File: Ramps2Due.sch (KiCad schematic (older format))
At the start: 24 parts, among them J1 HEADER_2, J10 HEADER_2, J11 HEADER_8, J12 HEADER_10, J13 HEADER_8, J14 HEADER_8, J15 HEADER_7, J2 HEADER_3X2, J3 HEADER_8, J4 HEADER_8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

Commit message: All the tracts added (I think)
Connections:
- net labels added: V_IN
- net labels removed: +12V, AM-VIN, AM_VIN
- wire segments 169 -> 172

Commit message: Add Open-Source Hardware logo, shrink board edges, remove extraneous tracts.
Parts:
- added M1: LOGO_OSHW, OSHW_logo_2, symbol LOGO_OSHW
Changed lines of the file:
@@
-EESchema Schematic File Version 2  date Thu 28 Feb 2013 03:48:15 PM EST
+EESchema Schematic File Version 2  date Thu 28 Feb 2013 05:09:04 PM EST
 LIBS:power
 LIBS:device
@@
 Comment4 ""
 $EndDescr
+$Comp
+L LOGO_OSHW M1
+U 1 1 512FD565
+P 7250 4600
+F 0 "M1" H 7250 4750 60  0000 C CNN
+F 1 "LOGO_OSHW" H 7250 4500 60  0000 C CNN
+F 2 "OSHW_logo_2" H 7150 4650 60  0000 C CNN
+	1    7250 4600
+	1    0    0    -1
+$EndComp
 Wire Wire Line
 	1000 4800 1150 4800

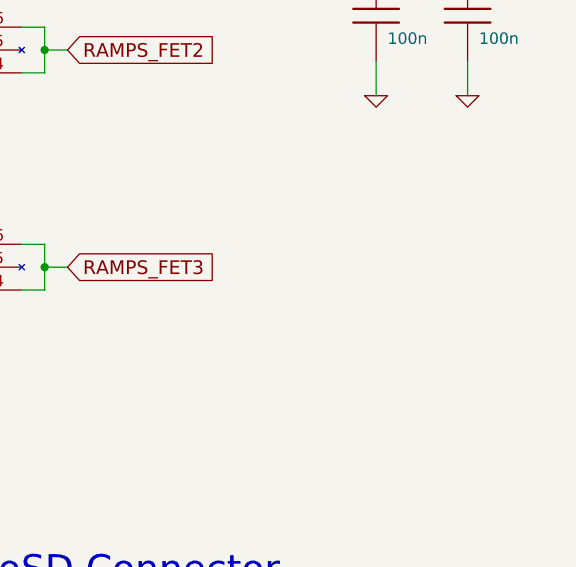
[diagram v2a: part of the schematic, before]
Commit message: Added spot for 5V pins to power endstops.
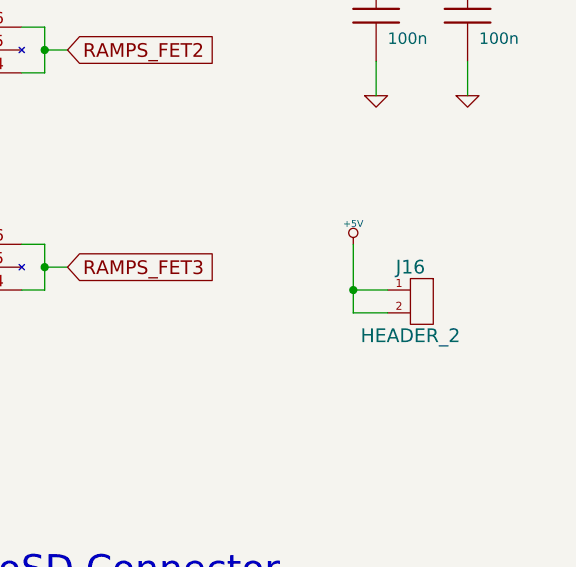
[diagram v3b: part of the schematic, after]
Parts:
- added J16: HEADER_2, symbol HEADER_2
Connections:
- wire segments 172 -> 175

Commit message: Rev0 complete. Sent to SeeedStudio for fabrication. Additionally, BOM added with suggested Digikey part numbers.
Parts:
- removed J1, J10: HEADER_2, symbol HEADER_2
- removed J6: HEADER_17X2, symbol HEADER_17X2
- added J1, J10: HEADER_2X2, symbol HEADER_2X2
- added J6: HEADER_16X2, symbol HEADER_16X2
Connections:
- net labels added: D22, D23
- wire segments 175 -> 180
- no-connect marks 30 -> 28
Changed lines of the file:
@@
-EESchema Schematic File Version 2  date Fri 01 Mar 2013 05:25:13 PM EST
+EESchema Schematic File Version 2  date Fri 01 Mar 2013 07:09:16 PM EST
 LIBS:power
 LIBS:device
@@
 Sheet 1 1
 Title ""
-Date "1 mar 2013"
+Date "2 mar 2013"
 Rev ""
 Comp ""
@@
 Comment4 ""
 $EndDescr
+Wire Wire Line
+	2250 2700 2100 2700
+Wire Wire Line
+	750  7150 500  7150
+Wire Wire Line
+	3250 3450 3050 3450
+Connection ~ 3350 3050
+Wire Wire Line
+	3350 3050 3350 2900
+Connection ~ 900  6750
+Wire Wire Line
+	750  7050 750  6750
+Wire Wire Line
+	750  6750 1050 6750
 Connection ~ 9950 3600
 Wire Wire Line
@@
 Wire Wire Line
 	5150 2700 4750 2700
-Connection ~ 3350 3000
-Wire Wire Line
-	3350 3000 3450 3000
-Wire Wire Line
-	3450 3000 3450 3150
 Wire Wire Line
 	4800 2100 5150 2100
@@
 	1400 5650 1250 5650
 Wire Wire Line
-	750  6900 750  6750
-Wire Wire Line
 	2100 7350 2350 7350
 Wire Wire Line
@@
 Wire Wire Line
 	2100 7450 2350 7450
-Wire Wire Line
-	850  6900 850  6750
-Wire Wire Line
-	850  6750 750  6750
-Connection ~ 800  6750
 Wire Wire Line
 	950  5750 850  5750
@@
 Wire Wire Line
 	5150 2000 4800 2000
-Wire Wire Line
-	3350 3150 3350 2900
 Wire Wire Line
 	4750 2600 5150 2600
@@
 	2850 2800 2850 2900
 Wire Wire Line
-	2550 2700 2750 2700
-Wire Wire Line
 	8200 6500 8200 5850
 Wire Wire Line
@@
 	8400 6250 8700 6250
 Wire Wire Line
-	2000 2700 2250 2700
-Wire Wire Line
 	7500 3200 7300 3200
 Wire Wire Line
@@
 Wire Wire Line
 	9950 3700 10100 3700
+Wire Wire Line
+	1050 6750 1050 7050
+Wire Wire Line
+	3550 3350 3550 3050
+Wire Wire Line
+	3550 3050 3250 3050
+Wire Wire Line
+	3250 3050 3250 3350
+Wire Wire Line
+	3550 3450 3650 3450
+Wire Wire Line
+	1050 7150 1150 7150
+Wire Wire Line
+	2700 2700 2550 2700
+Text Label 500  7150 0    60   ~ 0
+D22
+Text Label 1150 7150 0    60   ~ 0
+D23
+Text Label 3650 3450 0    60   ~ 0
+D23
+Text Label 3050 3450 0    60   ~ 0
+D22
+$Comp
+L HEADER_2X2 J1
+U 1 1 51313A3D
+P 900 7100
+F 0 "J1" H 900 7250 60  0000 C CNN
+F 1 "HEADER_2X2" H 900 6950 60  0000 C CNN
+	1    900  7100
+	1    0    0    -1
+$EndComp
+$Comp
+L HEADER_2X2 J10
+U 1 1 51313A27
+P 3400 3400
+F 0 "J10" H 3400 3550 60  0000 C CNN
+F 1 "HEADER_2X2" H 3400 3250 60  0000 C CNN
+	1    3400 3400
+	1    0    0    -1
+$EndComp
+$Comp
+L HEADER_16X2 J6
+U 1 1 513139D1
+P 2400 2050
+F 0 "J6" H 2400 2900 60  0000 C CNN
+F 1 "HEADER_16X2" H 2400 1200 60  0000 C CNN
+	1    2400 2050
+	1    0    0    -1
+$EndComp
+NoConn ~ 2250 1300
+NoConn ~ 2250 1400
+NoConn ~ 2250 1500
+NoConn ~ 2250 1600
+NoConn ~ 2250 1700
+NoConn ~ 2250 1800
 $Comp
 L +5V #PWR01
@@
 Text GLabel 8350 5650 0    60   Input ~ 0
 CD
-Text GLabel 2000 2700 0    60   Input ~ 0
+Text GLabel 2700 2700 2    60   Input ~ 0
 CD
 $Comp
@@
 Text GLabel 8350 5750 0    60   Output ~ 0
 MISO
-Text GLabel 2750 2700 2    60   Input ~ 0
+Text GLabel 2100 2700 0    60   Input ~ 0
 CS
 Text GLabel 8400 6250 0    60   Input ~ 0
@@
 NoConn ~ 2550 1400
 NoConn ~ 2550 1300
-NoConn ~ 2550 1200
-NoConn ~ 2250 1200
-NoConn ~ 2250 1300
-NoConn ~ 2250 1400
-NoConn ~ 2250 1500
-NoConn ~ 2250 1600
-NoConn ~ 2250 1700
-NoConn ~ 2250 1800
 NoConn ~ 2250 1900
 NoConn ~ 2250 2000
@@
 RAMPS_VCC
 $Comp
-L HEADER_2 J10
-U 1 1 512E96F5
-P 3400 3250
-F 0 "J10" H 3400 3400 60  0000 C CNN
-F 1 "HEADER_2" H 3400 3100 60  0000 C CNN
-	1    3400 3250
-	0    1    1    0
-$EndComp
-$Comp
 L HEADER_8 J14
 U 1 1 512E96E7
@@
 Text Notes 4200 900  0    120  ~ 0
 To RAMPS
-Text Notes 700  7250 0    60   ~ 0
+Text Notes 700  7500 0    60   ~ 0
 Note: This header\ngoes at the top\nof the 2X18 on\nthe Due
 $Comp
@@
 L +5V #PWR020
 U 1 1 512E9541
-P 800 6750
-F 0 "#PWR020" H 800 6840 20  0001 C CNN
-F 1 "+5V" H 800 6840 30  0000 C CNN
-	1    800  6750
-	1    0    0    -1
-$EndComp
-$Comp
-L HEADER_2 J1
-U 1 1 512E951A
-P 800 7000
-F 0 "J1" H 800 7150 60  0000 C CNN
-F 1 "HEADER_2" H 800 6850 60  0000 C CNN
-	1    800  7000
-	0    1    1    0
+P 900 6750
+F 0 "#PWR020" H 900 6840 20  0001 C CNN
+F 1 "+5V" H 900 6840 30  0000 C CNN
+	1    900  6750
+	1    0    0    -1
 $EndComp
 $Comp
@@
 Unaltered Headers
 $Comp
-L HEADER_17X2 J6
-U 1 1 512E8F43
-P 2400 2000
-F 0 "J6" H 2400 2900 60  0000 C CNN
-F 1 "HEADER_17X2" H 2400 1100 60  0000 C CNN
-	1    2400 2000
-	1    0    0    -1
-$EndComp
-$Comp
 L HEADER_8 J5
